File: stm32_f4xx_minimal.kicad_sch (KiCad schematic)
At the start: 45 parts, among them Q1 AO3401A, SW1 SW_SPDT, U1 MP2359DJ, U2 STM32F405RGT6, U3 W25N01GVZEIG_TR, Y1 16MHz

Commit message: updated schematic
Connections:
- net SPI2_CLK is gone; now on net SPI2_SCK: U3.6 (CLK)
- net SPI2_CS is gone; now on net SPI2_!CS: U3.1 (/CS)
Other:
- note added: "MCU"
- moved on the sheet: C1, C2, C3, C4, C5, C6, C7, C9, R1, Y1

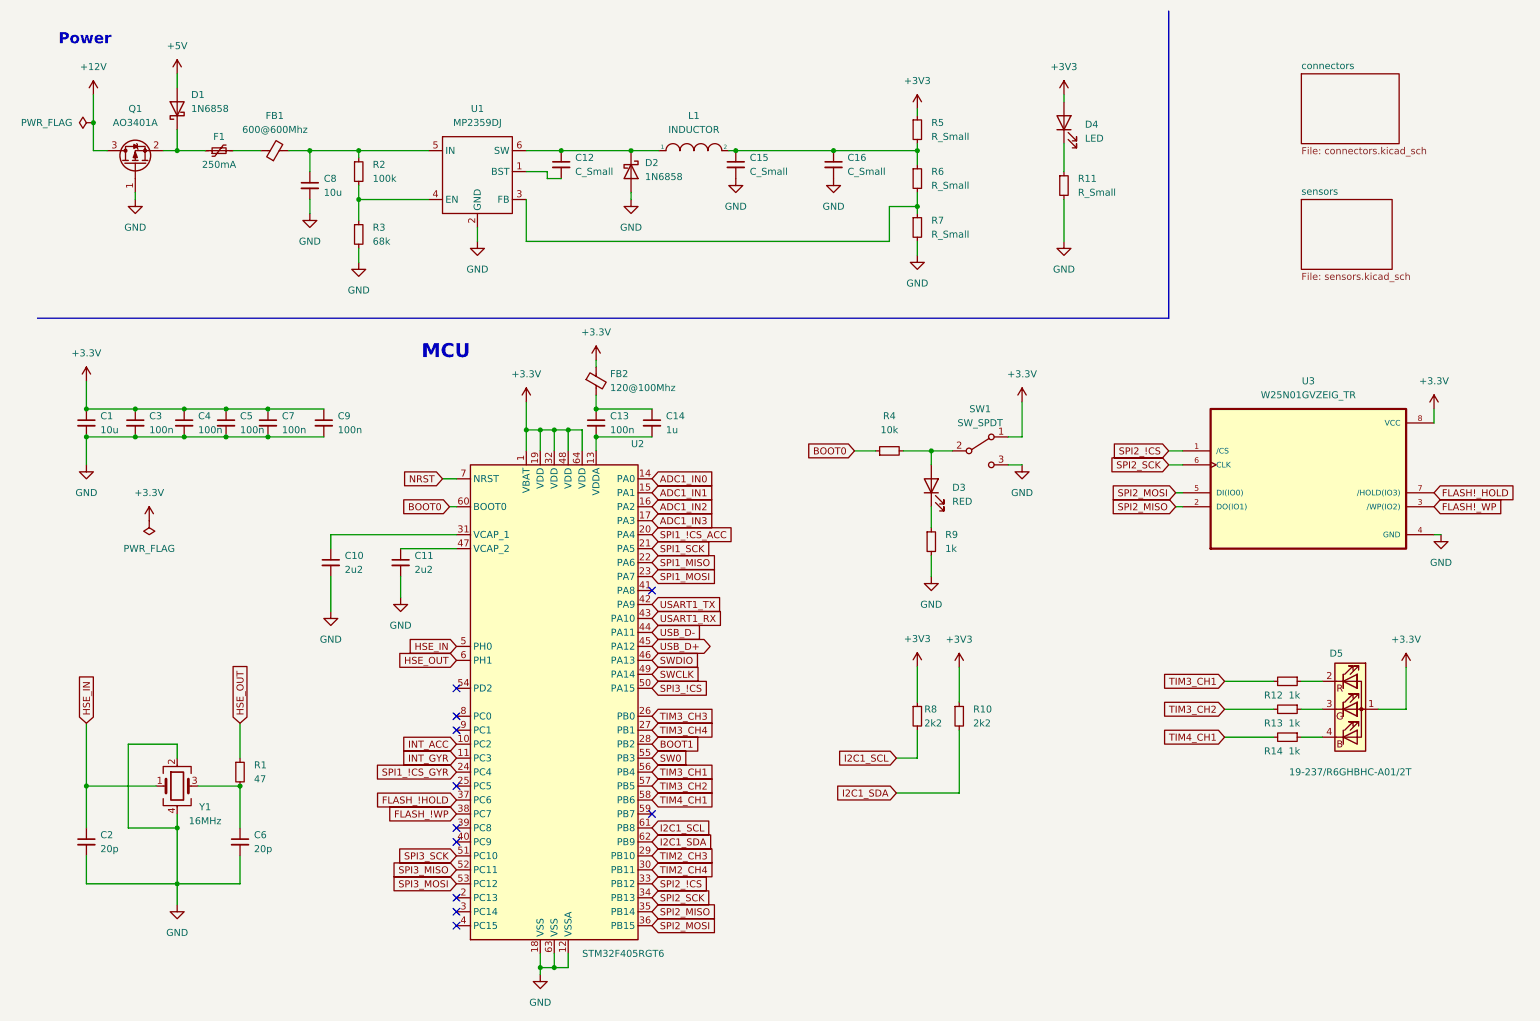
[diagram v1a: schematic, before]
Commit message: updated and parts placement
basic parts placement
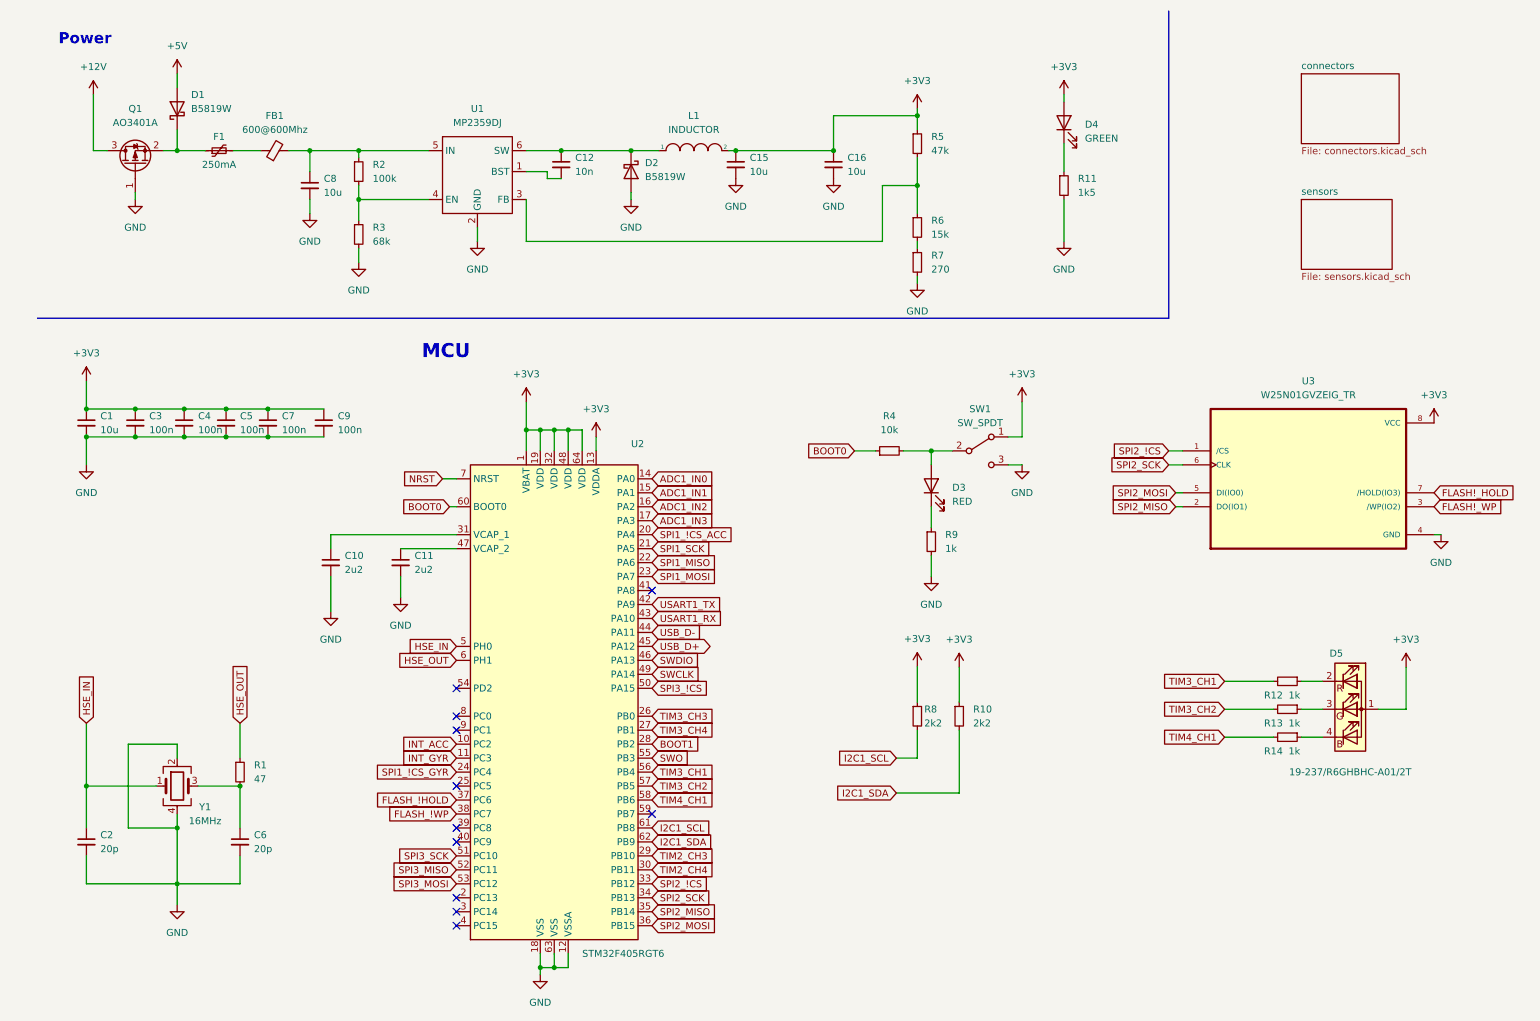
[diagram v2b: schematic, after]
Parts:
- removed C13: 100n, symbol Device:C_Small
- removed C14: 1u, symbol Device:C_Small
- removed FB2: 120@100Mhz, symbol Device:FerriteBead_Small
- C1, C8: footprint (none) -> Capacitor_SMD:C_1206_3216Metric
- C10, C11: footprint (none) -> Capacitor_SMD:C_0603_1608Metric
- C12: value C_Small -> 10n; footprint (none) -> Capacitor_SMD:C_0402_1005Metric
- C15, C16: value C_Small -> 10u; footprint (none) -> Capacitor_SMD:C_0603_1608Metric
- C2, C3, C4, C5, C6, C7, C9: footprint (none) -> Capacitor_SMD:C_0402_1005Metric
- D1, D2: value 1N6858 -> B5819W; footprint Diode_THT:D_DO-35_SOD27_P7.62mm_Horizontal -> B5819W-TP:SOD3716X135N
- D3: footprint (none) -> LED_SMD:LED_0603_1608Metric
- D4: value LED -> GREEN; footprint (none) -> LED_SMD:LED_0603_1608Metric
- D5: footprint (none) -> RGB_LED:19-237-R6GHBHC-A01-2T
- F1: footprint (none) -> Fuse:Fuse_1206_3216Metric
- FB1: footprint (none) -> Inductor_SMD:L_0805_2012Metric
- L1: footprint (none) -> Inductor_SMD:L_Sunlord_MWSA0518_5.4x5.2mm
- R1: footprint (none) -> Resistor_SMD:R_0402_1005Metric
- R10, R12, R13, R14, R2, R3, R4, R8, R9: footprint (none) -> Resistor_SMD:R_0603_1608Metric
- R11: value R_Small -> 1k5; footprint (none) -> Resistor_SMD:R_0603_1608Metric
- R5: value R_Small -> 47k; footprint (none) -> Resistor_SMD:R_0603_1608Metric
- R6: value R_Small -> 15k; footprint (none) -> Resistor_SMD:R_0603_1608Metric
- R7: value R_Small -> 270; footprint (none) -> Resistor_SMD:R_0603_1608Metric
- SW1: footprint (none) -> Button_Switch_SMD:SW_SPDT_PCM12
- U1: footprint (none) -> Package_TO_SOT_SMD:SOT-23-6
- U3: footprint SON127P800X600X80-9N -> WinbondFlash:W25N01GVZEIG
- Y1: footprint (none) -> Crystal:Crystal_SMD_3225-4Pin_3.2x2.5mm
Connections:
- net +3.3V is gone; now on net +3V3: C1.1, C3.1, C4.1, C5.1, C7.1, C9.1, D5.1 (A), SW1.1 (A), U2.1 (VBAT), U2.19 (VDD), U2.32 (VDD), U2.48 (VDD), U2.64 (VDD), U3.8 (VCC)
- net +3V3: now also C15.1, C16.1, L1.2, U2.13 (VDDA)
- net at R6.2, R7.1: no longer U1.3 (FB)
- net SW0 renamed SWO
- new net: R5.2, R6.1, U1.3 (FB)
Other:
- moved on the sheet: R5, R6, R7
